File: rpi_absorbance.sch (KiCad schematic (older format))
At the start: 33 parts, among them CON1 BARREL_JACK, P1 CONN_02X04, P2 CONN_01X02, P3 RPI_HEADER, P4 STEPPER_CONN, P5 CONN_02X05, Q1 ZTX692B, U1 R-78B5.0-1.5L, U2 MUN5216DW1T1G, U3 DRV8825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

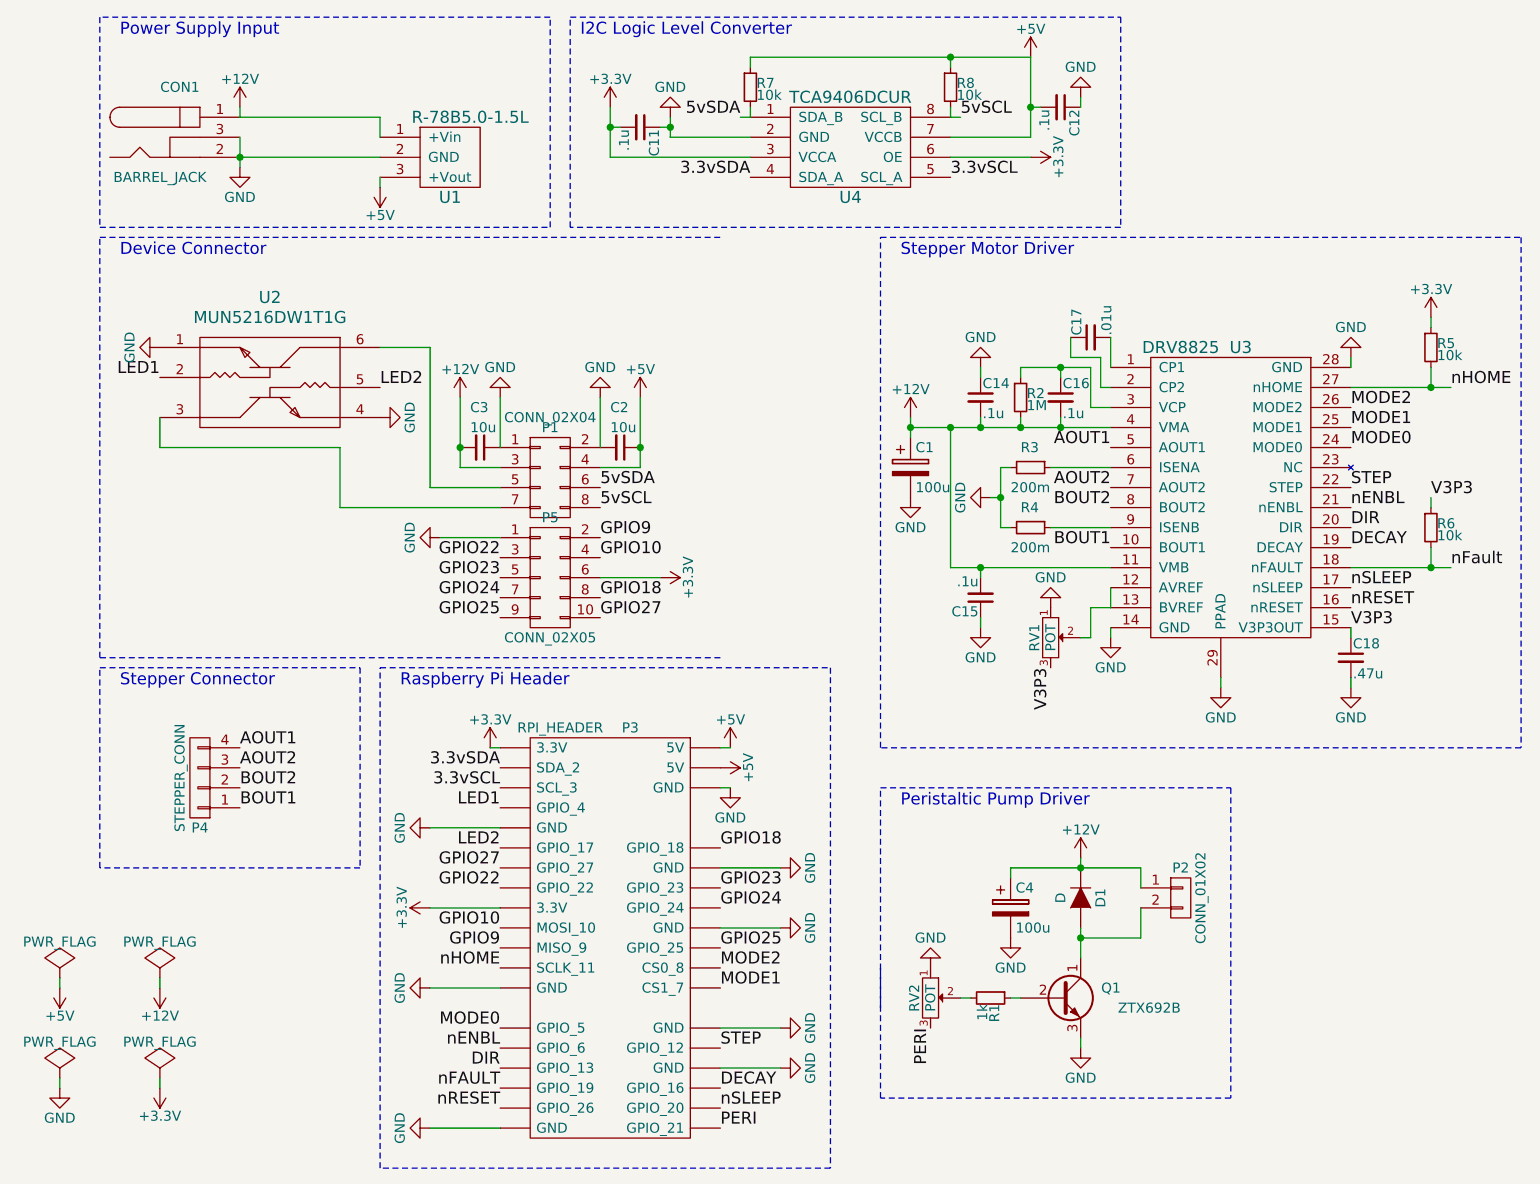
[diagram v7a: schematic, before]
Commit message: Add labels and outline
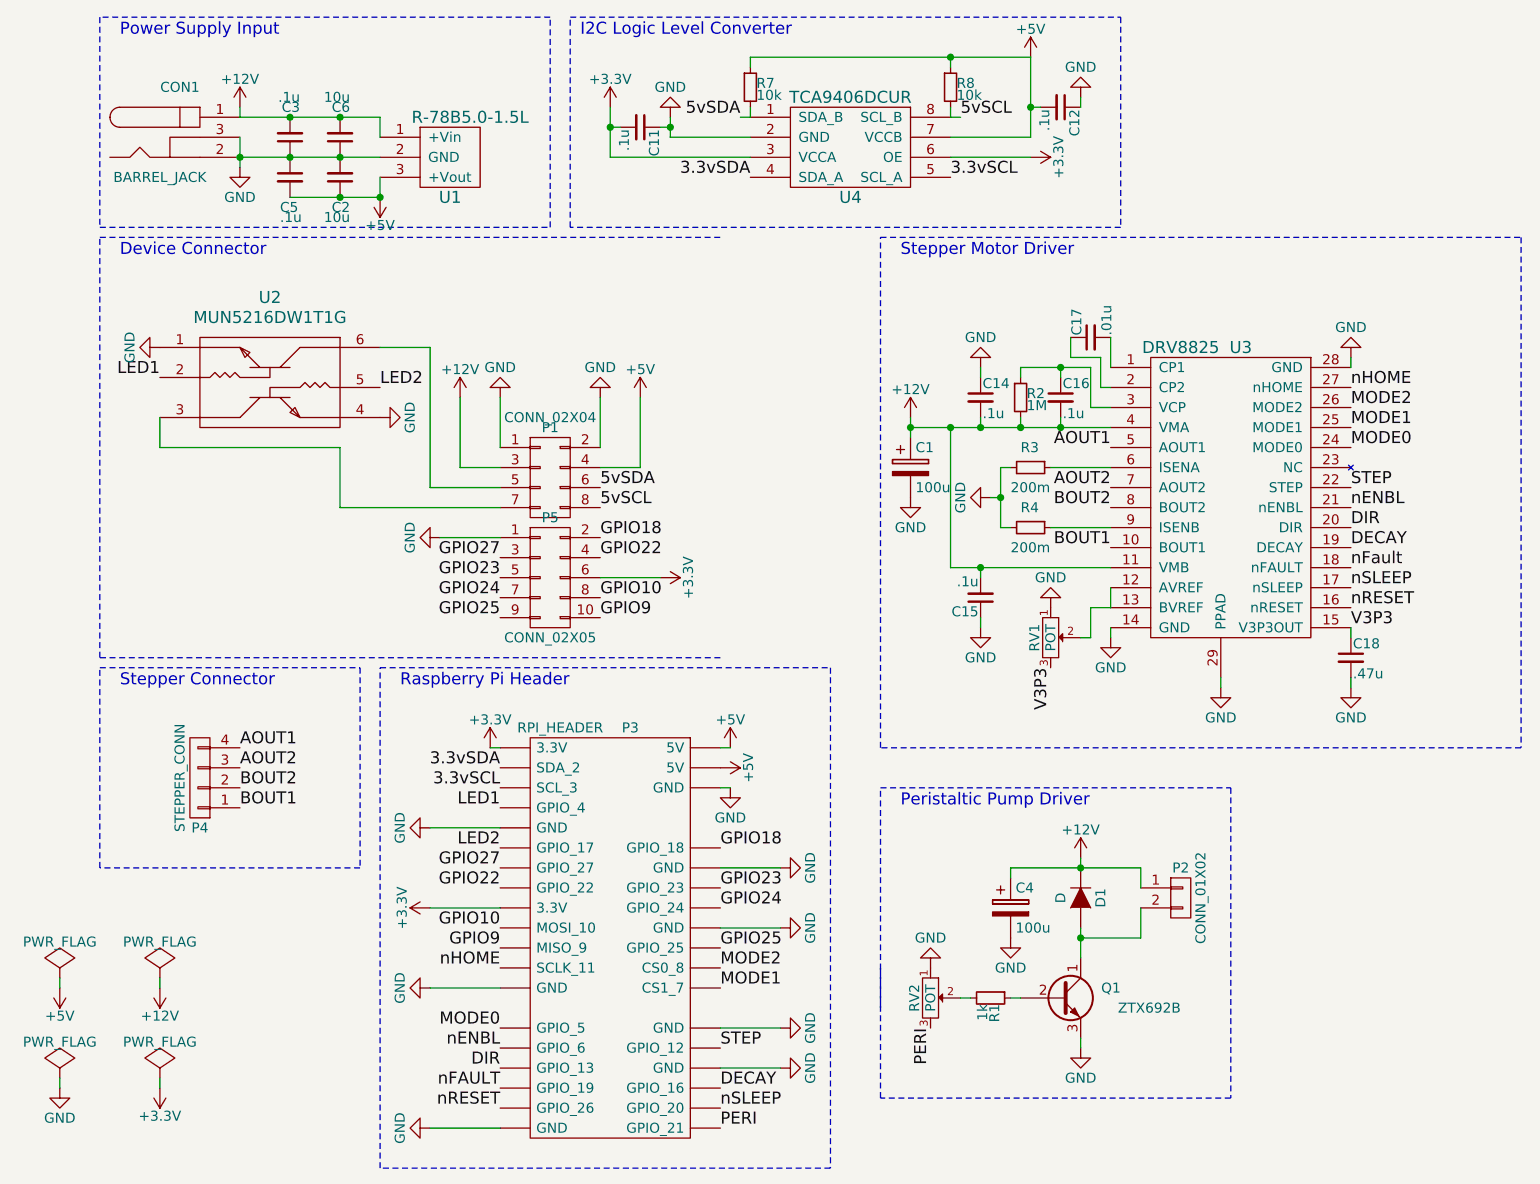
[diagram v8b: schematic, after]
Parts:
- removed R5, R6: 10k, Resistors_SMD:R_0603, symbol R_Small
- added C5: .1u, Capacitors_SMD:C_0603, symbol C_Small
- added C6: 10u, Capacitors_SMD:C_0603, symbol C_Small
- C3: value 10u -> .1u
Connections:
- net +12V: now also C6.2
- net +5V: now also C5.2
- net GND: now also C5.1, C6.1
- net GPIO10: now also P5.8 (P8); no longer P5.4 (P4)
- net GPIO18: now also P5.2 (P2); no longer P5.8 (P8)
- net GPIO22: now also P5.4 (P4); no longer P5.3 (P3)
- net GPIO27: now also P5.3 (P3); no longer P5.10 (P10)
- net GPIO9: now also P5.10 (P10); no longer P5.2 (P2)
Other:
- moved on the sheet: C2, C3
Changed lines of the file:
@@
 L C_Small C2
 U 1 1 56CB7DA5
-P 3700 3750
-F 0 "C2" V 3500 3700 50  0000 L CNN
-F 1 "10u" V 3600 3700 50  0000 L CNN
-F 2 "Capacitors_SMD:C_0603" H 3700 3750 50  0001 C CNN
-F 3 "" H 3700 3750 50  0000 C CNN
-	1    3700 3750
-	0    1    1    0
+P 2300 2400
+F 0 "C2" H 2250 2550 50  0000 L CNN
+F 1 "10u" H 2250 2600 50  0000 L CNN
+F 2 "Capacitors_SMD:C_0603" H 2300 2400 50  0001 C CNN
+F 3 "" H 2300 2400 50  0000 C CNN
+	1    2300 2400
+	-1   0    0    1
 $EndComp
 Text Label 5400 2100 0    60   ~ 0
@@
 L +5V #PWR04
 U 1 1 56CB9603
-P 2500 2450
-F 0 "#PWR04" H 2500 2300 50  0001 C CNN
-F 1 "+5V" H 2500 2590 50  0000 C CNN
-F 2 "" H 2500 2450 50  0000 C CNN
-F 3 "" H 2500 2450 50  0000 C CNN
-	1    2500 2450
+P 2500 2500
+F 0 "#PWR04" H 2500 2350 50  0001 C CNN
+F 1 "+5V" H 2500 2640 50  0000 C CNN
+F 2 "" H 2500 2500 50  0000 C CNN
+F 3 "" H 2500 2500 50  0000 C CNN
+	1    2500 2500
 	-1   0    0    1
 $EndComp
@@
 L C_Small C3
 U 1 1 56CB9979
-P 3000 3750
-F 0 "C3" V 2800 3700 50  0000 L CNN
-F 1 "10u" V 2900 3700 50  0000 L CNN
-F 2 "Capacitors_SMD:C_0603" H 3000 3750 50  0001 C CNN
-F 3 "" H 3000 3750 50  0000 C CNN
-	1    3000 3750
-	0    1    1    0
+P 2050 2200
+F 0 "C3" H 2000 2050 50  0000 L CNN
+F 1 ".1u" H 2000 2000 50  0000 L CNN
+F 2 "Capacitors_SMD:C_0603" H 2050 2200 50  0001 C CNN
+F 3 "" H 2050 2200 50  0000 C CNN
+	1    2050 2200
+	-1   0    0    1
 $EndComp
 $Comp
@@
 	1    0    0    -1
 $EndComp
-$Comp
-L R_Small R5
-U 1 1 56CD219E
-P 7750 3250
-F 0 "R5" H 7780 3270 50  0000 L CNN
-F 1 "10k" H 7780 3210 50  0000 L CNN
-F 2 "Resistors_SMD:R_0603" H 7750 3250 50  0001 C CNN
-F 3 "" H 7750 3250 50  0000 C CNN
-	1    7750 3250
-	1    0    0    -1
-$EndComp
-Text Label 7850 3450 0    60   ~ 0
+Text Label 7350 3450 0    60   ~ 0
 nHOME
-Text Label 7850 4350 0    60   ~ 0
+Text Label 7350 4350 0    60   ~ 0
 nFault
-$Comp
-L R_Small R6
-U 1 1 56CD266C
-P 7750 4150
-F 0 "R6" H 7780 4170 50  0000 L CNN
-F 1 "10k" H 7780 4110 50  0000 L CNN
-F 2 "Resistors_SMD:R_0603" H 7750 4150 50  0001 C CNN
-F 3 "" H 7750 4150 50  0000 C CNN
-	1    7750 4150
-	1    0    0    -1
-$EndComp
-Text Label 7750 4000 0    60   ~ 0
-V3P3
 Text Label 7350 4250 0    60   ~ 0
 DECAY
@@
 PERI
 $Comp
-L GND #PWR043
+L GND #PWR041
 U 1 1 56D00D89
 P 5650 6200
-F 0 "#PWR043" H 5650 5950 50  0001 C CNN
+F 0 "#PWR041" H 5650 5950 50  0001 C CNN
 F 1 "GND" H 5650 6050 50  0000 C CNN
 F 2 "" H 5650 6200 50  0000 C CNN
@@
 $EndComp
 $Comp
-L +12V #PWR044
+L +12V #PWR042
 U 1 1 56D01707
 P 6000 5800
-F 0 "#PWR044" H 6000 5650 50  0001 C CNN
+F 0 "#PWR042" H 6000 5650 50  0001 C CNN
 F 1 "+12V" H 6000 5940 50  0000 C CNN
 F 2 "" H 6000 5800 50  0000 C CNN
@@
 $EndComp
 $Comp
-L GND #PWR045
+L GND #PWR043
 U 1 1 56D018B9
 P 6000 6750
-F 0 "#PWR045" H 6000 6500 50  0001 C CNN
+F 0 "#PWR043" H 6000 6500 50  0001 C CNN
 F 1 "GND" H 6000 6600 50  0000 C CNN
 F 2 "" H 6000 6750 50  0000 C CNN
@@
 PERI
 $Comp
-L +12V #PWR046
+L +12V #PWR044
 U 1 1 56D24636
 P 2900 3500
-F 0 "#PWR046" H 2900 3350 50  0001 C CNN
+F 0 "#PWR044" H 2900 3350 50  0001 C CNN
 F 1 "+12V" H 2900 3640 50  0000 C CNN
 F 2 "" H 2900 3500 50  0000 C CNN
@@
 $EndComp
 $Comp
-L GND #PWR047
+L GND #PWR045
 U 1 1 56D248DC
 P 3600 3500
-F 0 "#PWR047" H 3600 3250 50  0001 C CNN
+F 0 "#PWR045" H 3600 3250 50  0001 C CNN
 F 1 "GND" H 3600 3350 50  0000 C CNN
 F 2 "" H 3600 3500 50  0000 C CNN
@@
 $EndComp
 $Comp
-L GND #PWR048
+L GND #PWR046
 U 1 1 56D251E1
 P 3100 3500
-F 0 "#PWR048" H 3100 3250 50  0001 C CNN
+F 0 "#PWR046" H 3100 3250 50  0001 C CNN
 F 1 "GND" H 3100 3350 50  0000 C CNN
 F 2 "" H 3100 3500 50  0000 C CNN
@@
 LED2
 $Comp
-L GND #PWR049
+L GND #PWR047
 U 1 1 56D2C382
 P 2800 4200
-F 0 "#PWR049" H 2800 3950 50  0001 C CNN
+F 0 "#PWR047" H 2800 3950 50  0001 C CNN
 F 1 "GND" H 2800 4050 50  0000 C CNN
 F 2 "" H 2800 4200 50  0000 C CNN
@@
 Text Label 3100 6250 2    60   ~ 0
 GPIO9
-Text Label 3600 4300 0    60   ~ 0
+Text Label 3600 4500 0    60   ~ 0
 GPIO10
-Text Label 3600 4200 0    60   ~ 0
+Text Label 3600 4600 0    60   ~ 0
 GPIO9
 $Comp
@@
 $EndComp
 $Comp
-L GND #PWR050
+L GND #PWR048
 U 1 1 56D3407A
 P 1400 3250
-F 0 "#PWR050" H 1400 3000 50  0001 C CNN
+F 0 "#PWR048" H 1400 3000 50  0001 C CNN
 F 1 "GND" H 1400 3100 50  0000 C CNN
 F 2 "" H 1400 3250 50  0000 C CNN
@@
 $EndComp
 $Comp
-L GND #PWR051
+L GND #PWR049
 U 1 1 56D340E8
 P 2500 3600
-F 0 "#PWR051" H 2500 3350 50  0001 C CNN
+F 0 "#PWR049" H 2500 3350 50  0001 C CNN
 F 1 "GND" H 2500 3450 50  0000 C CNN
 F 2 "" H 2500 3600 50  0000 C CNN
@@
 $EndComp
 $Comp
-L GND #PWR052
+L GND #PWR050
 U 1 1 56D3711B
 P 5250 6350
-F 0 "#PWR052" H 5250 6100 50  0001 C CNN
+F 0 "#PWR050" H 5250 6100 50  0001 C CNN
 F 1 "GND" H 5250 6200 50  0000 C CNN
 F 2 "" H 5250 6350 50  0000 C CNN
@@
 F 3 "" H 3350 2700 50  0000 C CNN
 	1    3350 3900
-	1    0    0    -1
-$EndComp
-$Comp
-L +3.3V #PWR053
-U 1 1 56D4F704
-P 7750 3100
-F 0 "#PWR053" H 7750 2950 50  0001 C CNN
-F 1 "+3.3V" H 7750 3240 50  0000 C CNN
-F 2 "" H 7750 3100 50  0000 C CNN
-F 3 "" H 7750 3100 50  0000 C CNN
-	1    7750 3100
 	1    0    0    -1
 $EndComp
@@
 GPIO18
 Connection ~ 1800 2300
-Connection ~ 3800 3750
 Wire Wire Line
 	2500 2100 2500 2200
@@
 Wire Wire Line
 	1800 2300 2500 2300
-Connection ~ 2900 3750
 Wire Notes Line
 	4750 4850 4750 7350
@@
 Wire Wire Line
 	7350 4950 7350 4900
-Wire Wire Line
-	7350 3450 7850 3450
-Wire Wire Line
-	7350 4350 7850 4350
-Wire Wire Line
-	7750 3350 7750 3450
-Connection ~ 7750 3450
-Wire Wire Line
-	7750 3150 7750 3100
-Wire Wire Line
-	7750 4250 7750 4350
-Connection ~ 7750 4350
-Wire Wire Line
-	7750 4050 7750 4000
 Wire Notes Line
 	5000 2700 8200 2700
@@
 	3800 3850 3600 3850
 Wire Wire Line
-	2500 2450 2500 2400
+	2500 2500 2500 2400
 $Comp
 L CONN_02X05 P5
@@
 	1    0    0    -1
 $EndComp
-Text Label 3600 4500 0    60   ~ 0
+Text Label 3600 4200 0    60   ~ 0
 GPIO18
 Text Label 3100 4400 2    60   ~ 0
@@
 Wire Wire Line
 	3900 4400 3600 4400
-Text Label 3600 4600 0    60   ~ 0
+Text Label 3100 4300 2    60   ~ 0
 GPIO27
 Text Label 3100 5950 2    60   ~ 0
@@
 Text Label 3100 5850 2    60   ~ 0
 GPIO27
-Text Label 3100 4300 2    60   ~ 0
+Text Label 3600 4300 0    60   ~ 0
 GPIO22
+Connection ~ 2050 2300
+Connection ~ 2050 2100
+Wire Wire Line
+	2050 2500 2500 2500
+Connection ~ 2500 2500
+$Comp
+L C_Small C6
+U 1 1 56D62C47
+P 2300 2200
+F 0 "C6" H 2250 2050 50  0000 L CNN
+F 1 "10u" H 2250 2000 50  0000 L CNN
+F 2 "Capacitors_SMD:C_0603" H 2300 2200 50  0001 C CNN
+F 3 "" H 2300 2200 50  0000 C CNN
+	1    2300 2200
+	-1   0    0    1
+$EndComp
+Connection ~ 2300 2300
+Connection ~ 2300 2100
+$Comp
+L C_Small C5
+U 1 1 56D62E8A
+P 2050 2400
+F 0 "C5" H 2000 2250 50  0000 L CNN
+F 1 ".1u" H 2000 2200 50  0000 L CNN
+F 2 "Capacitors_SMD:C_0603" H 2050 2400 50  0001 C CNN
+F 3 "" H 2050 2400 50  0000 C CNN
+	1    2050 2400
+	1    0    0    -1
+$EndComp
+Connection ~ 2300 2500
 $EndSCHEMATC
